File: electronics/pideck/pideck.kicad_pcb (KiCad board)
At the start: 2 copper layers, 60.1 x 42.7 mm, 50 parts, among them J1 BM20B_0.8_-34DS-0.4V_53_, Q1 RE1C002UNTCL, Q2 RE1C002UNTCL, Q3 RE1C002UNTCL, Q4 RE1C002UNTCL, Q5 RE1C002UNTCL, Q6 RE1C002UNTCL, Q7 RE1C002UNTCL, Q8 RE1C002UNTCL, U1 RP2040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

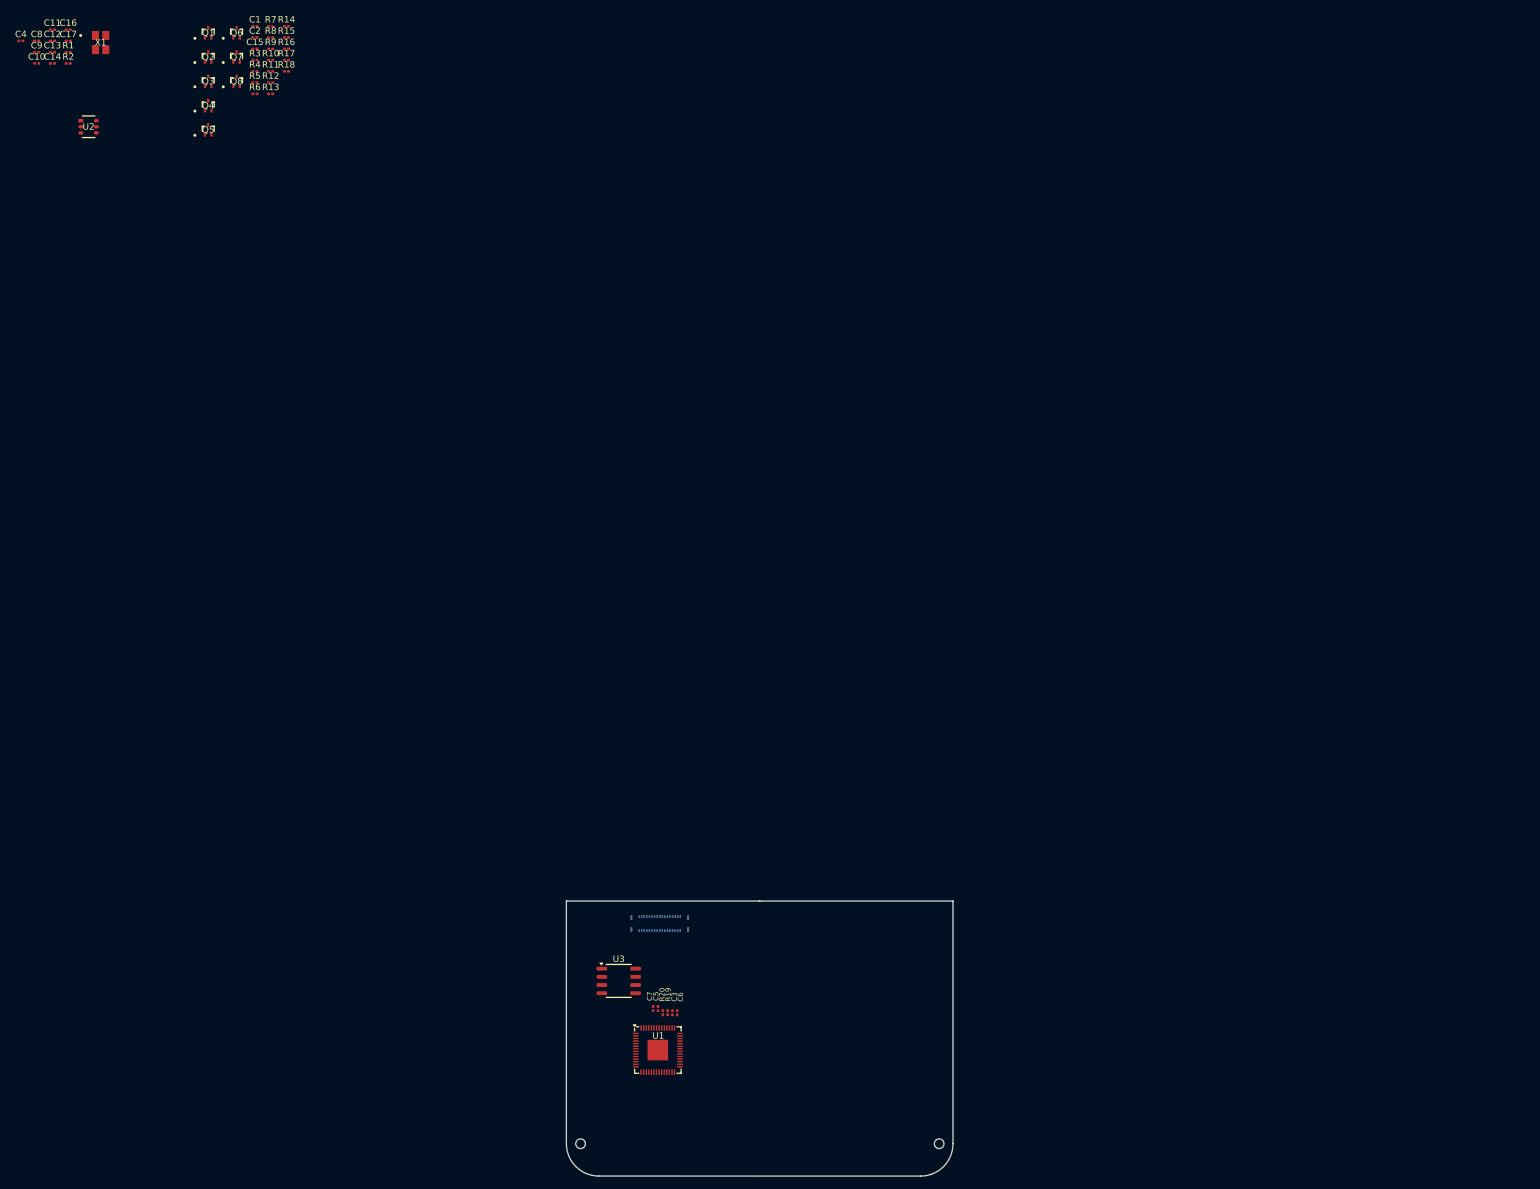
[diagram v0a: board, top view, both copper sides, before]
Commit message: Adding ethernet, hdmi, and battery to CM5
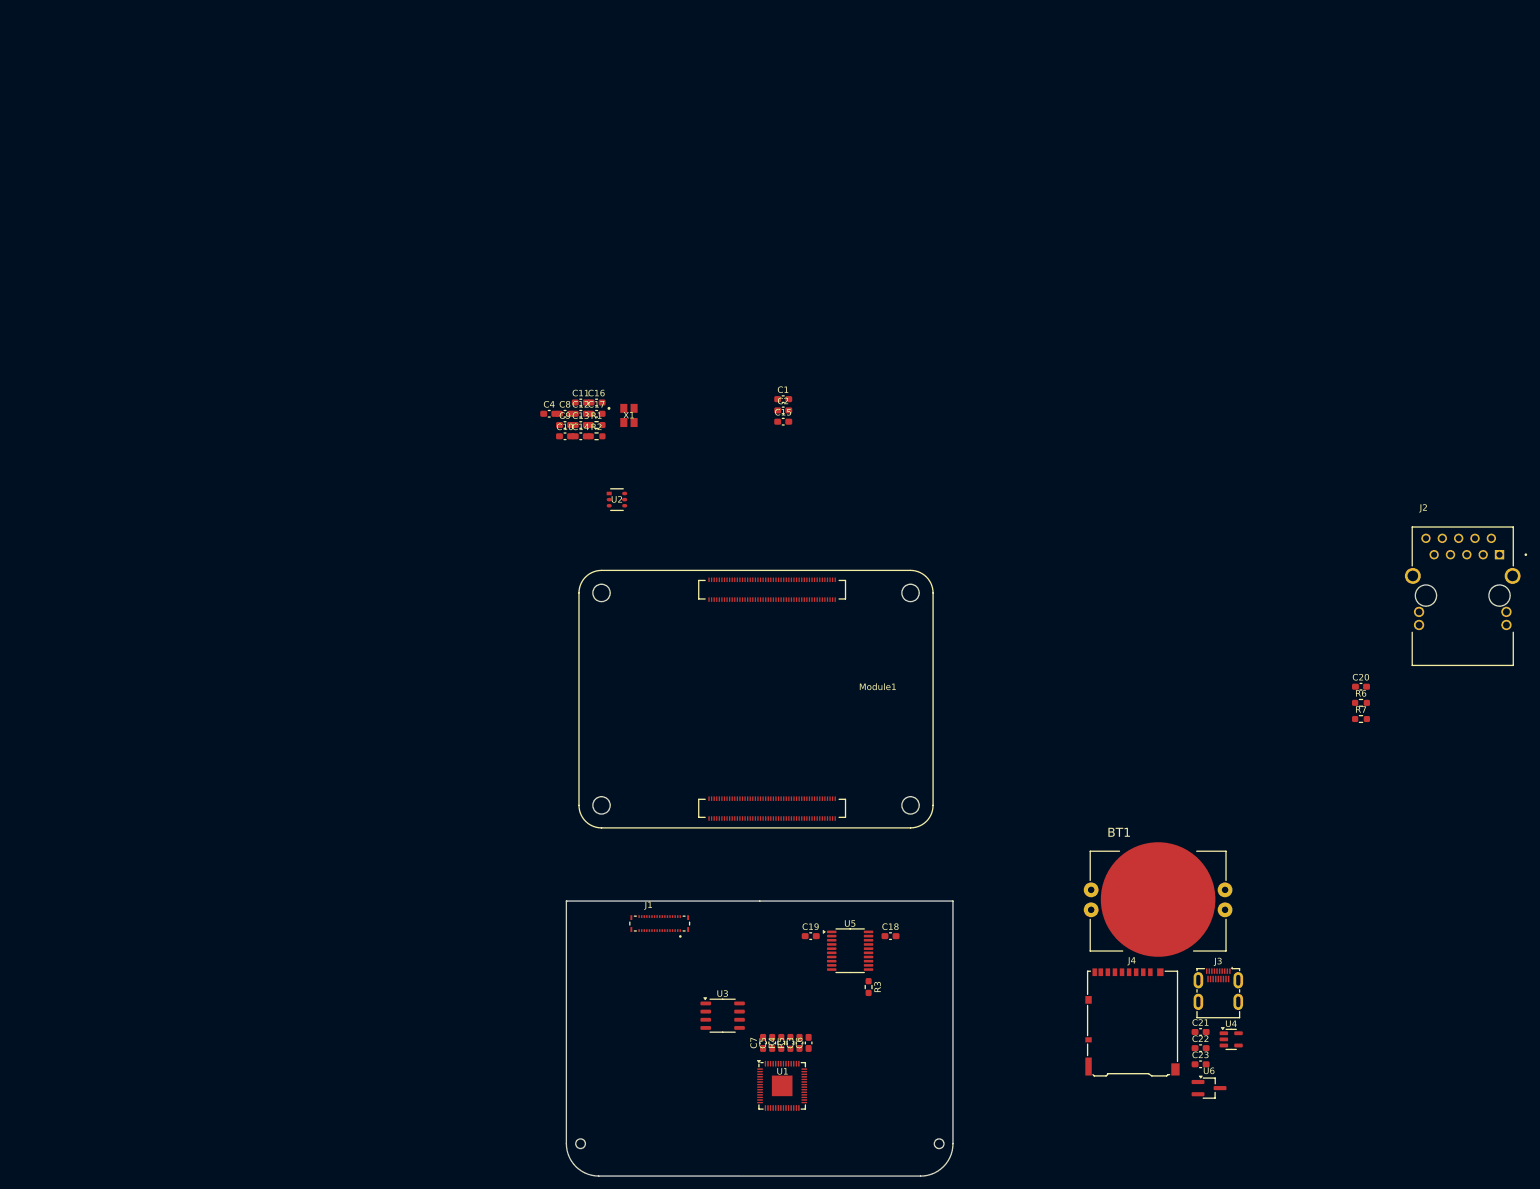
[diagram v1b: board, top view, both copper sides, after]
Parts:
- removed Q1, Q2, Q3, Q4, Q5, Q6, Q7, Q8: RE1C002UNTCL, RE1C002UNTCL:DIO_RB558WMF_ROM
- removed R10, R11, R12, R13, R14, R15, R16, R17, R18, R8, R9: 10K, Resistor_SMD:R_0201_0603Metric
- removed the R4 at (19.3, -3.58)
- removed the R5 at (19.3, -1.83)
- added BT1: BAT-HLD-001-THM, BAT-HLD-001-THM:BAT_BAT-HLD-001-THM, F.Cu at (159.6, 125.1)
- added C18: 1uF, Capacitor_SMD:C_0603_1608Metric_Pad1.08x0.95mm_HandSolder, F.Cu at (118.1, 130.8)
- added C19: 1uF, Capacitor_SMD:C_0603_1608Metric_Pad1.08x0.95mm_HandSolder, F.Cu at (105.7, 130.8)
- added C20: 100nF, Capacitor_SMD:C_0603_1608Metric_Pad1.08x0.95mm_HandSolder, F.Cu at (191.2, 92.0)
- added C21: 10uF, Capacitor_SMD:C_0603_1608Metric_Pad1.08x0.95mm_HandSolder, F.Cu at (166.2, 145.6)
- added C22: 100nF, Capacitor_SMD:C_0603_1608Metric_Pad1.08x0.95mm_HandSolder, F.Cu at (166.2, 148.2)
- added C23: 100nF, Capacitor_SMD:C_0603_1608Metric_Pad1.08x0.95mm_HandSolder, F.Cu at (166.2, 150.7)
- added J2: ARJM11D7-502-AB-EW2, ARJM11D7-502-AB-EW2:ABRACON_ARJM11D7-502-AB-EW2, F.Cu at (207.0, 77.8)
- added J3: HDMI_D_1.4, Connector_Video:HDMI_Micro-D_Molex_46765-1x01, F.Cu at (169.0, 141.0)
- added J4: Micro_SD_Card_Det2, Connector_Card:microSD_HC_Hirose_DM3AT-SF-PEJM5, F.Cu at (155.7, 144.1)
- added Module1: ComputeModule5-CM5, CM5IO:Raspberry-Pi-5-Compute-Module, F.Cu at (121.2, 110.4)
- added U4: RT9742GGJ5, Package_TO_SOT_SMD:SOT-23-5, F.Cu at (171.0, 146.8)
- added U5: TXS0108EPW, Package_SO:TSSOP-20_4.4x6.5mm_P0.65mm, F.Cu at (111.8, 133.0)
- added U6: RT9742SNGV, Package_TO_SOT_SMD:TSOT-23_HandSoldering, F.Cu at (167.6, 154.4)
- C1, C10, C11, C12, C13, C14, C15, C16, C17, C2, C3, C4, C5, C6, C7, C8, C9: footprint Capacitor_SMD:C_0201_0603Metric -> Capacitor_SMD:C_0603_1608Metric_Pad1.08x0.95mm_HandSolder
- J1: moved to F.Cu
- R1, R2, R3: footprint Resistor_SMD:R_0201_0603Metric -> Resistor_SMD:R_0603_1608Metric_Pad0.98x0.95mm_HandSolder
- R4: renamed from R20; footprint Resistor_SMD:R_0201_0603Metric -> Resistor_SMD:R_0603_1608Metric_Pad0.98x0.95mm_HandSolder
- R5: renamed from R19; footprint Resistor_SMD:R_0201_0603Metric -> Resistor_SMD:R_0603_1608Metric_Pad0.98x0.95mm_HandSolder
- R6, R7: value 10K -> 470; footprint Resistor_SMD:R_0201_0603Metric -> Resistor_SMD:R_0603_1608Metric_Pad0.98x0.95mm_HandSolder
- moved R7 200.7 mm to (191.2, 97.0)
- moved R6 196.1 mm to (191.2, 94.5)
- moved R3 172.7 mm to (114.7, 138.7), turned to -90 degrees
- moved C1 100.5 mm to (101.4, 47.3)
- moved C10 100.5 mm to (67.5, 53.1)
- moved C11 100.5 mm to (70.0, 47.9)
- moved C12 100.5 mm to (70.0, 49.6)
- moved C13 100.5 mm to (70.0, 51.4)
- moved C14 100.5 mm to (70.0, 53.1)
- moved C15 100.5 mm to (101.4, 50.8)
- moved C16 100.5 mm to (72.4, 47.9)
- moved C17 100.5 mm to (72.4, 49.6)
- moved C2 100.5 mm to (101.4, 49.1)
- moved C4 100.5 mm to (65.1, 49.6)
- moved C8 100.5 mm to (67.5, 49.6)
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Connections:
- R3 pad 1: KB_BLK_LED_A -> GND
- R3 pad 2: KB_BLK_LED_K_3V3 -> +1V8
- R6 pad 1: KB_BLK_LED_A -> ETH_LEDG
- R6 pad 2: PANNEL_BLK_LED_K_3V3 -> Net-(J2-PadP12)
- R7 pad 1: +1V8 -> ETH_LEDY
- R7 pad 2: TP_BLK_LED_K_1V8 -> Net-(J2-PadP14)

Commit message: added usb
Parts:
- turned R4 to -90 degrees
- turned R5 to -90 degrees
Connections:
- Module1 pad 103: unconnected-(Module1B-USB2_N-Pad103) -> KB_USB_D-
- Module1 pad 105: unconnected-(Module1B-USB2_P-Pad105) -> KB_USB_D+
- R4 pad 1: /USB_D+ -> KB_USB_D+
- R5 pad 1: /USB_D- -> KB_USB_D-
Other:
- board size 60.1 x 42.7 mm -> 60.1 x 97.1 mm
